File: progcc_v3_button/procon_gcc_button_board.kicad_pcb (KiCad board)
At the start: 4 copper layers, 110 x 54.3 mm, 32 parts, among them J1 To Button Board, J2 bumpers, SW1 TL3315NF100Q, SW10 DPAD, SW11 DPAD, SW12 DPAD, SW2 TL3315NF100Q, SW3 TL3315NF100Q, SW4 TL3315NF100Q, SW5 BPAD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

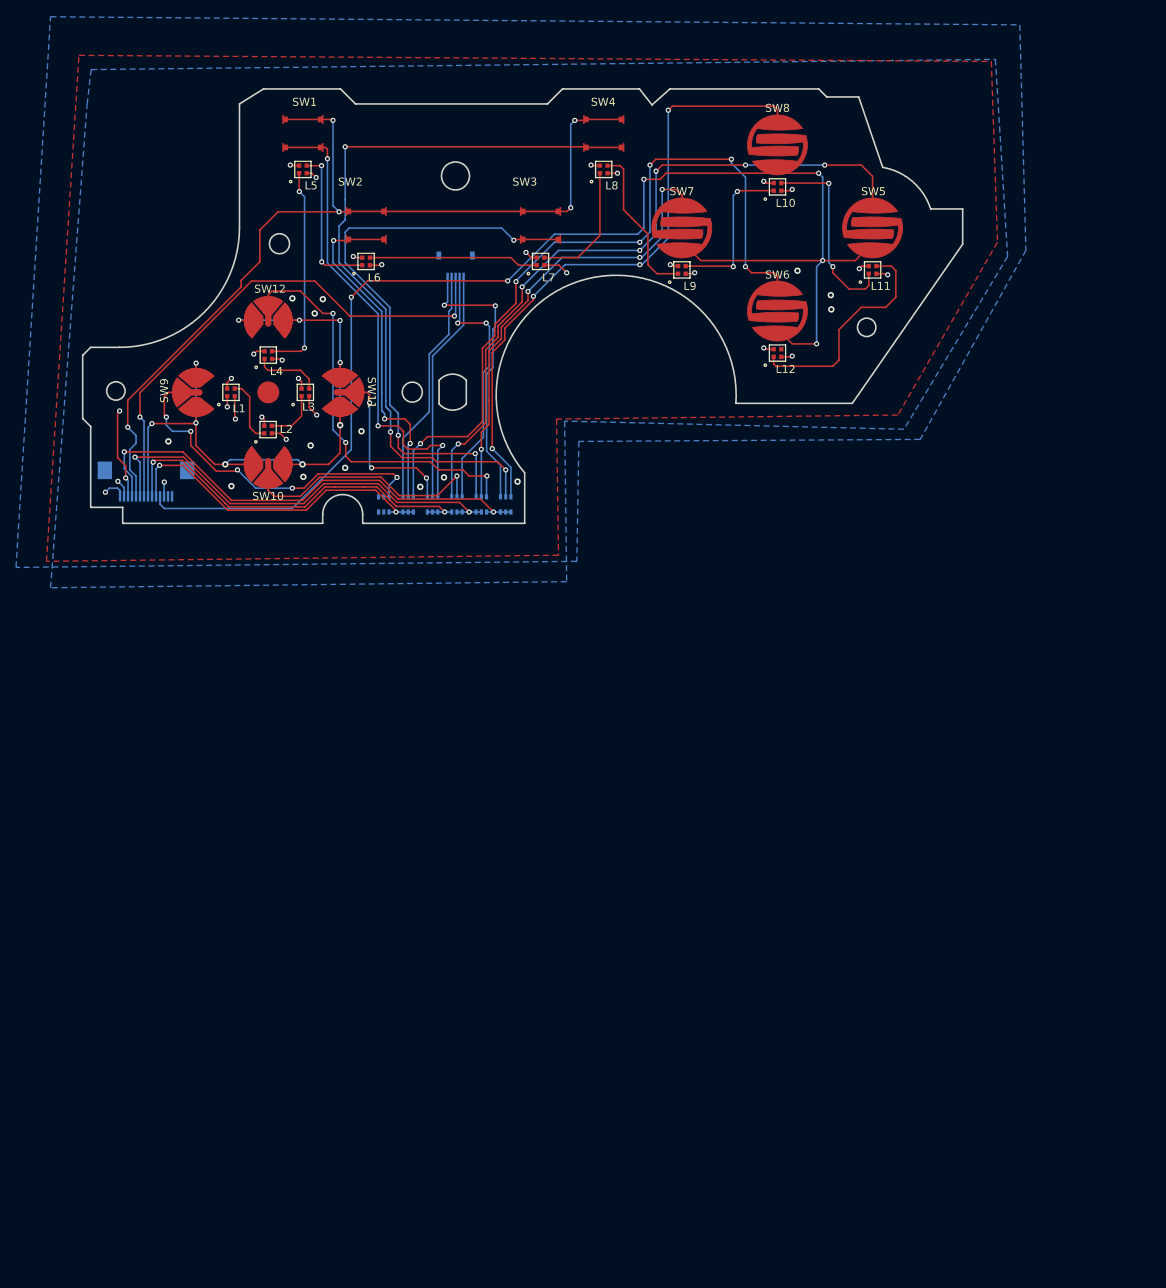
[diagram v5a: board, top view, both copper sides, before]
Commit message: Major updates
-Revised button board outline
-Added IMU for motion
-Cleaned up traces on main board
-Add test pads to button board
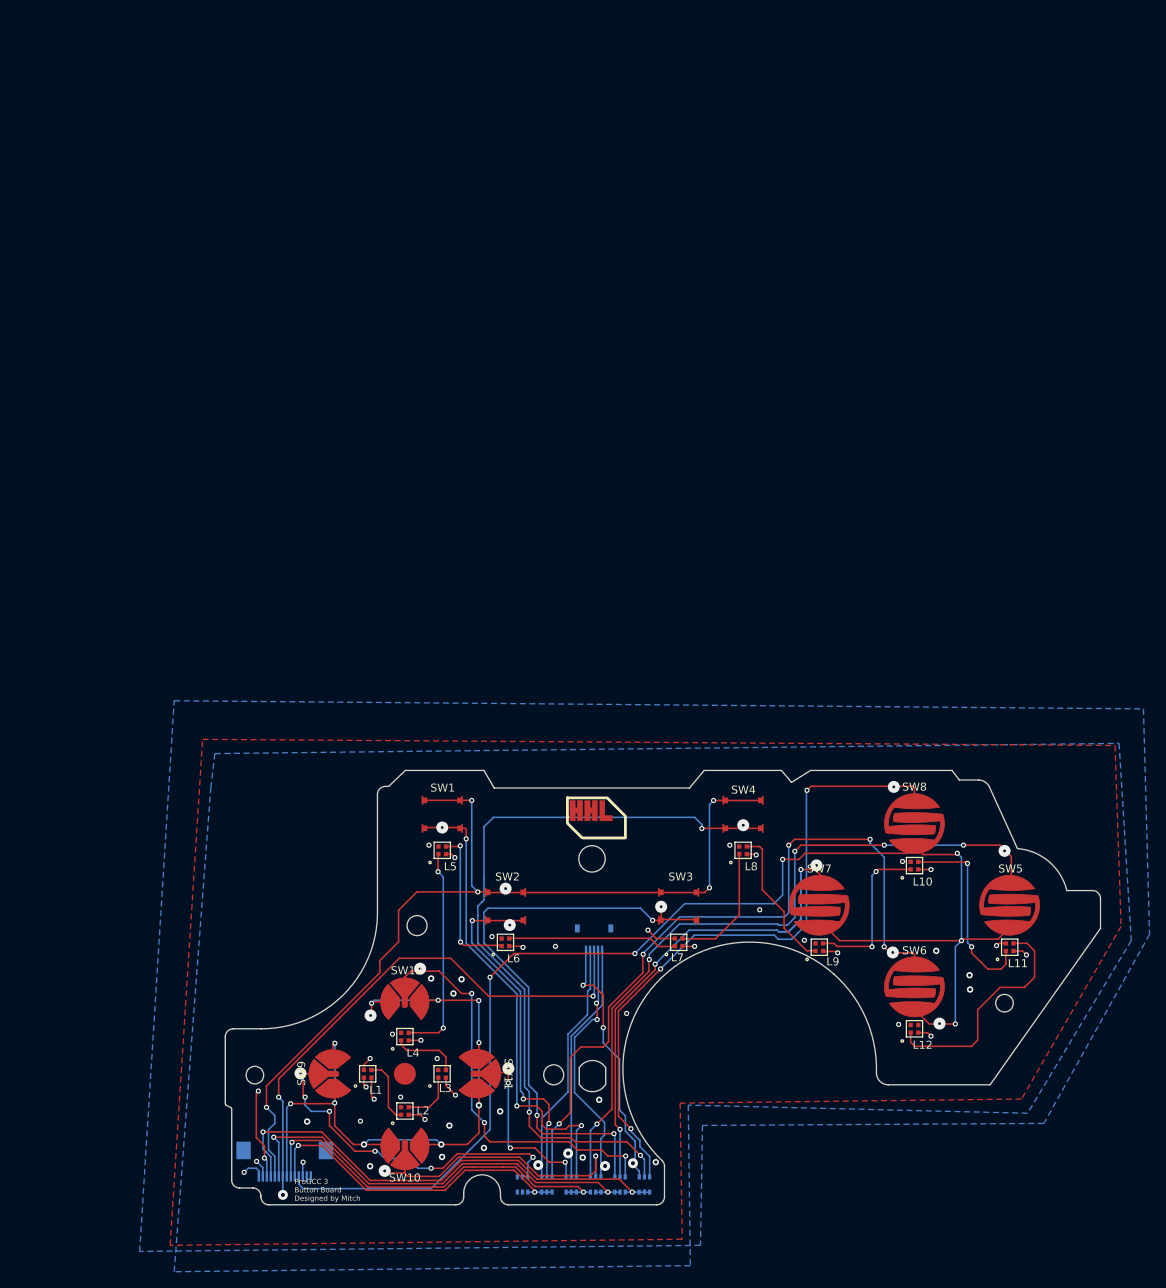
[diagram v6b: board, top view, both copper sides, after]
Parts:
- added REF**: HHL_Logo, progcc_v3:HHL_Logo, F.Cu at (142.7, 118.9)
- D1, D2, D3, D4, D5, D6: footprint Package_TO_SOT_SMD:SOT-363_SC-70-6 -> progcc_v3:SOT-363_SC-70-6
- J2: footprint progcc_v3:molex_5051100592_5P -> progcc_v3:molex_5034800540
- moved SW1 89.1 mm to (124.1, 118.0)
- moved SW4 89.1 mm to (161.7, 118.0)
- moved SW2 89.1 mm to (132.0, 129.5)
- moved SW3 89.0 mm to (153.7, 129.5)
- moved SW12 86.9 mm to (119.5, 141.4)
- moved L4 86.9 mm to (119.5, 145.8)
- moved L2 86.9 mm to (119.5, 155.1)
- moved SW10 86.9 mm to (119.5, 159.4)
- moved L1 86.9 mm to (114.8, 150.4)
- moved L3 86.9 mm to (124.1, 150.4)
- moved SW11 86.9 mm to (128.5, 150.4)
- moved SW9 86.9 mm to (110.5, 150.4)
- moved L5 86.9 mm to (124.1, 122.5)
- moved L6 86.9 mm to (132.0, 134.0)
- moved L8 86.9 mm to (161.7, 122.5)
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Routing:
- net GND: track 20.4 -> 11.7 mm, vias 29 -> 33
- net DD_Pull: track 30.4 -> 34.4 mm, vias 1 -> 2
- net Scan_B: track 90.0 -> 93.5 mm, vias 10 -> 11
- net X_Pull: track 79.7 -> 83.0 mm
- net Scan_D: track 65.1 -> 68.1 mm, vias 2 -> 3
- net ZL_Pull: track 35.2 -> 32.2 mm, vias 2 -> 3
- net Y_Pull: track 57.7 -> 60.0 mm
- net Home_Pull: track 72.6 -> 74.3 mm, vias 3 -> 4
- net BPAD_RGB: track 19.6 -> 18.2 mm
- net A_Pull: track 89.4 -> 90.7 mm
- net Net-(L11-DOUT): track 28.1 -> 29.1 mm
- net R_Pull: track 32.7 -> 31.8 mm, vias 2 -> 3
- net ZR_Pull: track 29.1 -> 30.0 mm, vias 0 -> 1
- net L_Pull: track 30.0 -> 30.9 mm, vias 0 -> 1
- net Plus_Pull: track 94.0 -> 94.7 mm, vias 3 -> 4
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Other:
- board size 110 x 54.3 mm -> 109.4 x 54.3 mm
- board text added: "ProGCC 3 Button Board Designed by Mitch"
